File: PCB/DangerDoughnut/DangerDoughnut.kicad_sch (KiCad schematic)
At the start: 81 parts, among them J1 Conn_01x02_Pin, J2 Conn_01x02_Pin, J3 Conn_01x02_Pin, J4 Conn_01x04_Pin, J6 USB_C_Receptacle_USB2.0_16P, U1 MMC5983MA, U10 ESP32-S3, U2 H3LIS331DLTR, U3 H3LIS331DLTR, U4 W25X20CLZP, U6 L5973D, U7 MIC5219-3.3YM5, U8 ESP8285H16, U9 SX1280IMLTRT, Y1 40MHz, Y2 52MHz, Y3 26MHz

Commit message: verified elsr
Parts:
- removed FL2: 2450FM07D0034T, Danger_Doughnut_Lib:FIL_2450FM07D0034T, symbol Danger_Doughnut_Lib:2450FM07D0034T
- removed R11: 0, Resistor_SMD:R_0603_1608Metric_Pad0.98x0.95mm_HandSolder, symbol Device:R
- added C29: 100uF, Capacitor_THT:CP_Radial_D6.3mm_P2.50mm, symbol Device:C_Polarized
- added D6: Green LED, LED_SMD:LED_0805_2012Metric, symbol Device:LED
- added R20: 30, Resistor_SMD:R_0402_1005Metric, symbol Device:R
- added R21, R22: 100, Resistor_SMD:R_0402_1005Metric, symbol Device:R
- C1, C11, C14, C16, C17, C2, C20, C21, C22, C23, C25, C26, C27, C28, C3, C30, C32, C33, C6, C7, C9: footprint Capacitor_SMD:C_0603_1608Metric_Pad1.08x0.95mm_HandSolder -> Capacitor_SMD:C_0402_1005Metric
- C8: footprint Capacitor_SMD:CP_Elec_6.3x7.7 -> Capacitor_THT:CP_Radial_D6.3mm_P2.50mm
- D2: footprint Diode_SMD:D_SOD-882D -> Diode_SMD:D_0805_2012Metric
- D3: footprint Diode_SMD:D_SOD-882D -> Capacitor_SMD:C_0805_2012Metric
- R1, R10, R12, R13, R14, R15, R16, R19, R2, R3, R4, R5, R6, R7, R8, R9: footprint Resistor_SMD:R_0603_1608Metric_Pad0.98x0.95mm_HandSolder -> Resistor_SMD:R_0402_1005Metric
- R17, R18: value 2.2K -> 3.3k; footprint Resistor_SMD:R_0603_1608Metric_Pad0.98x0.95mm_HandSolder -> Resistor_SMD:R_0402_1005Metric
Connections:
- net +3.3V: now also C21.1, U9.11 (VBAT_IO), R20.2
- net +5V: now also J4.3 (Pin_3); no longer J4.2 (Pin_2)
- net +BATT: now also C29.1
- net GND: now also J4.4 (Pin_4), C29.2; no longer J4.1 (Pin_1)
- net LED_MOSI: now also R21.2
- net LED_SCK: now also R22.2
- net ACCEL2_INT: now reaches U3.11 (INT1)
- net MAG_INT: now reaches U1.15 (INT)
- net ACCEL1_INT: now reaches U2.11 (INT1)
- new net: D6.2 (A), R20.1
- new net: J4.1 (Pin_1), R22.1
- new net: J4.2 (Pin_2), R21.1
- new net LED_BOTTOM: D6.1 (K)
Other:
- note added: "TODO: wire ESP32 uart resistor? find pinouts sensor interupts? add pin header add disconnects add test points add ground option elrs boot pin boot pins accessable Organize"
- note removed: "TODO: import HD107s LEDs wire LEDs wire ESP32 uart resistor? find pinouts sensor interupts? add pin header add disconnects add test points boot pins accessable Organize"

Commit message: updated schematic
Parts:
- added C34: 1.8pF, Capacitor_SMD:C_0402_1005Metric, symbol Device:C
- added C35: 1.2pF, Capacitor_SMD:C_0402_1005Metric, symbol Device:C
- added C36: 1uF, Capacitor_SMD:C_0402_1005Metric, symbol Device:C
- added C41: 100nF, Capacitor_SMD:C_0603_1608Metric, symbol Device:C
- added L3: 3nH, Inductor_SMD:L_0402_1005Metric_Pad0.77x0.64mm_HandSolder, symbol Device:L
- added R11: 10K, Resistor_SMD:R_0402_1005Metric, symbol Device:R
- added R25: 510, Resistor_SMD:R_0402_1005Metric, symbol Device:R
- added SW1, SW2: SW_Push, Button_Switch_SMD:SW_Push_1P1T_XKB_TS-1187A, symbol Switch:SW_Push
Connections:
- net +3.3V: now also R11.1
- net ACCEL1_INT: now also U10.8 (GPIO3)
- net ACCEL2_INT: now also U10.7 (GPIO2)
- net Accel1_CS: now also U10.11 (GPIO6)
- net Accel2_CS: now also U10.12 (GPIO7)
- net ELSR_RX: now also R25.2
- net ELSR_TX: now also U10.50 (U0RXD)
- net GND: now also C34.2, C35.2, C36.2, SW2.1
- net LED_BOTTOM: now also U10.16 (GPIO11)
- net MAG_INT: now also U10.9 (GPIO4)
- net Mag_CS: now also U10.10 (GPIO5)
- net at U10.1 (LNA_IN): now also C34.1, L3.1
- net ESP_RST: now reaches U10.4 (CHIP_PU)
- net ESP_RST: now also C36.1, C41.1, R11.2, SW1.1
- net at U10.49 (U0TXD): now also R25.1
- net at U10.5 (GPIO0): now also SW2.2
- net at ANT2.2 (FEED): now also C35.1, L3.2
- new net: C41.2, SW1.2
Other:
- note added: "TODO: add pin header add disconnects add test points add ground option elrs boot pin boot pins accessable Organize"
- note removed: "TODO: wire ESP32 uart resistor? find pinouts sensor interupts? add pin header add disconnects add test points add ground option elrs boot pin boot pins accessable Organize"
- moved on the sheet: ANT2

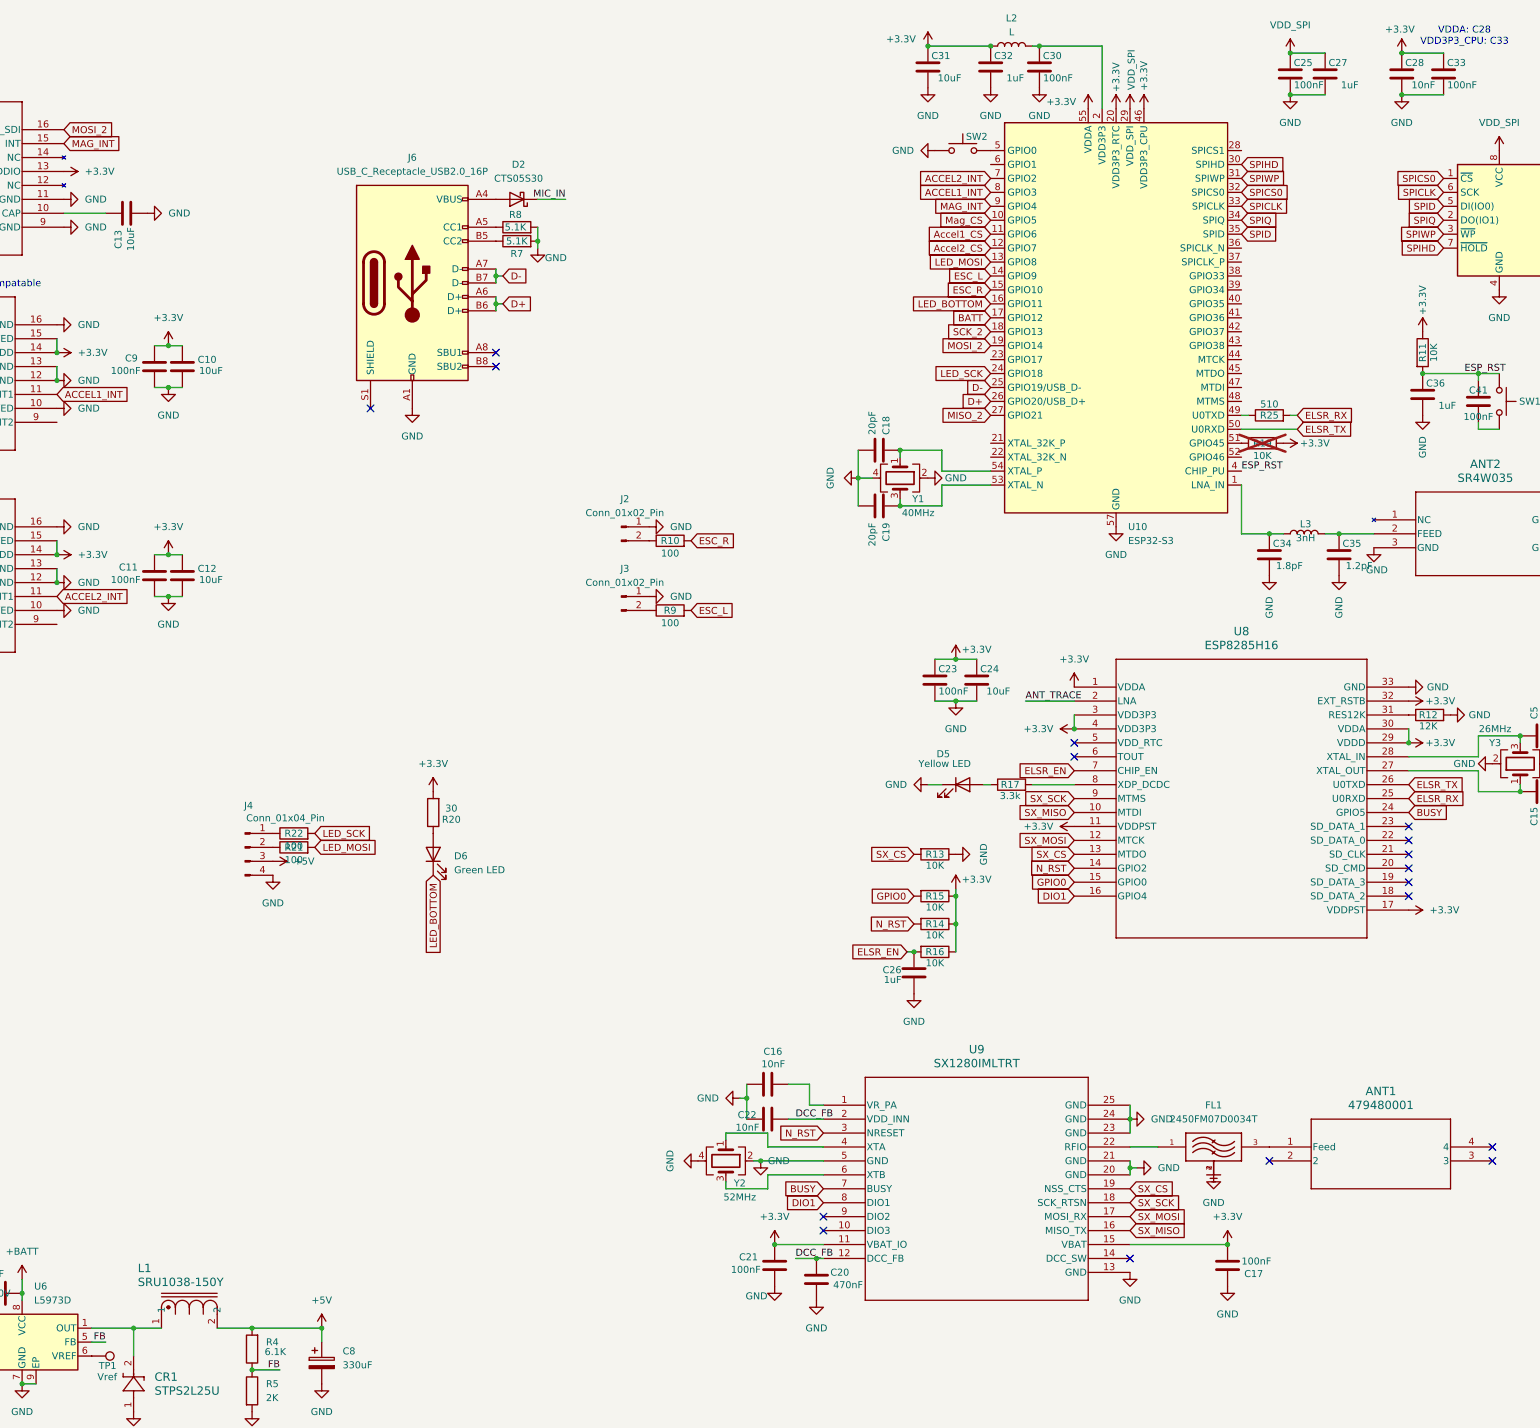
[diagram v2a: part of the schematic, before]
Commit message: updated schematic power layout done
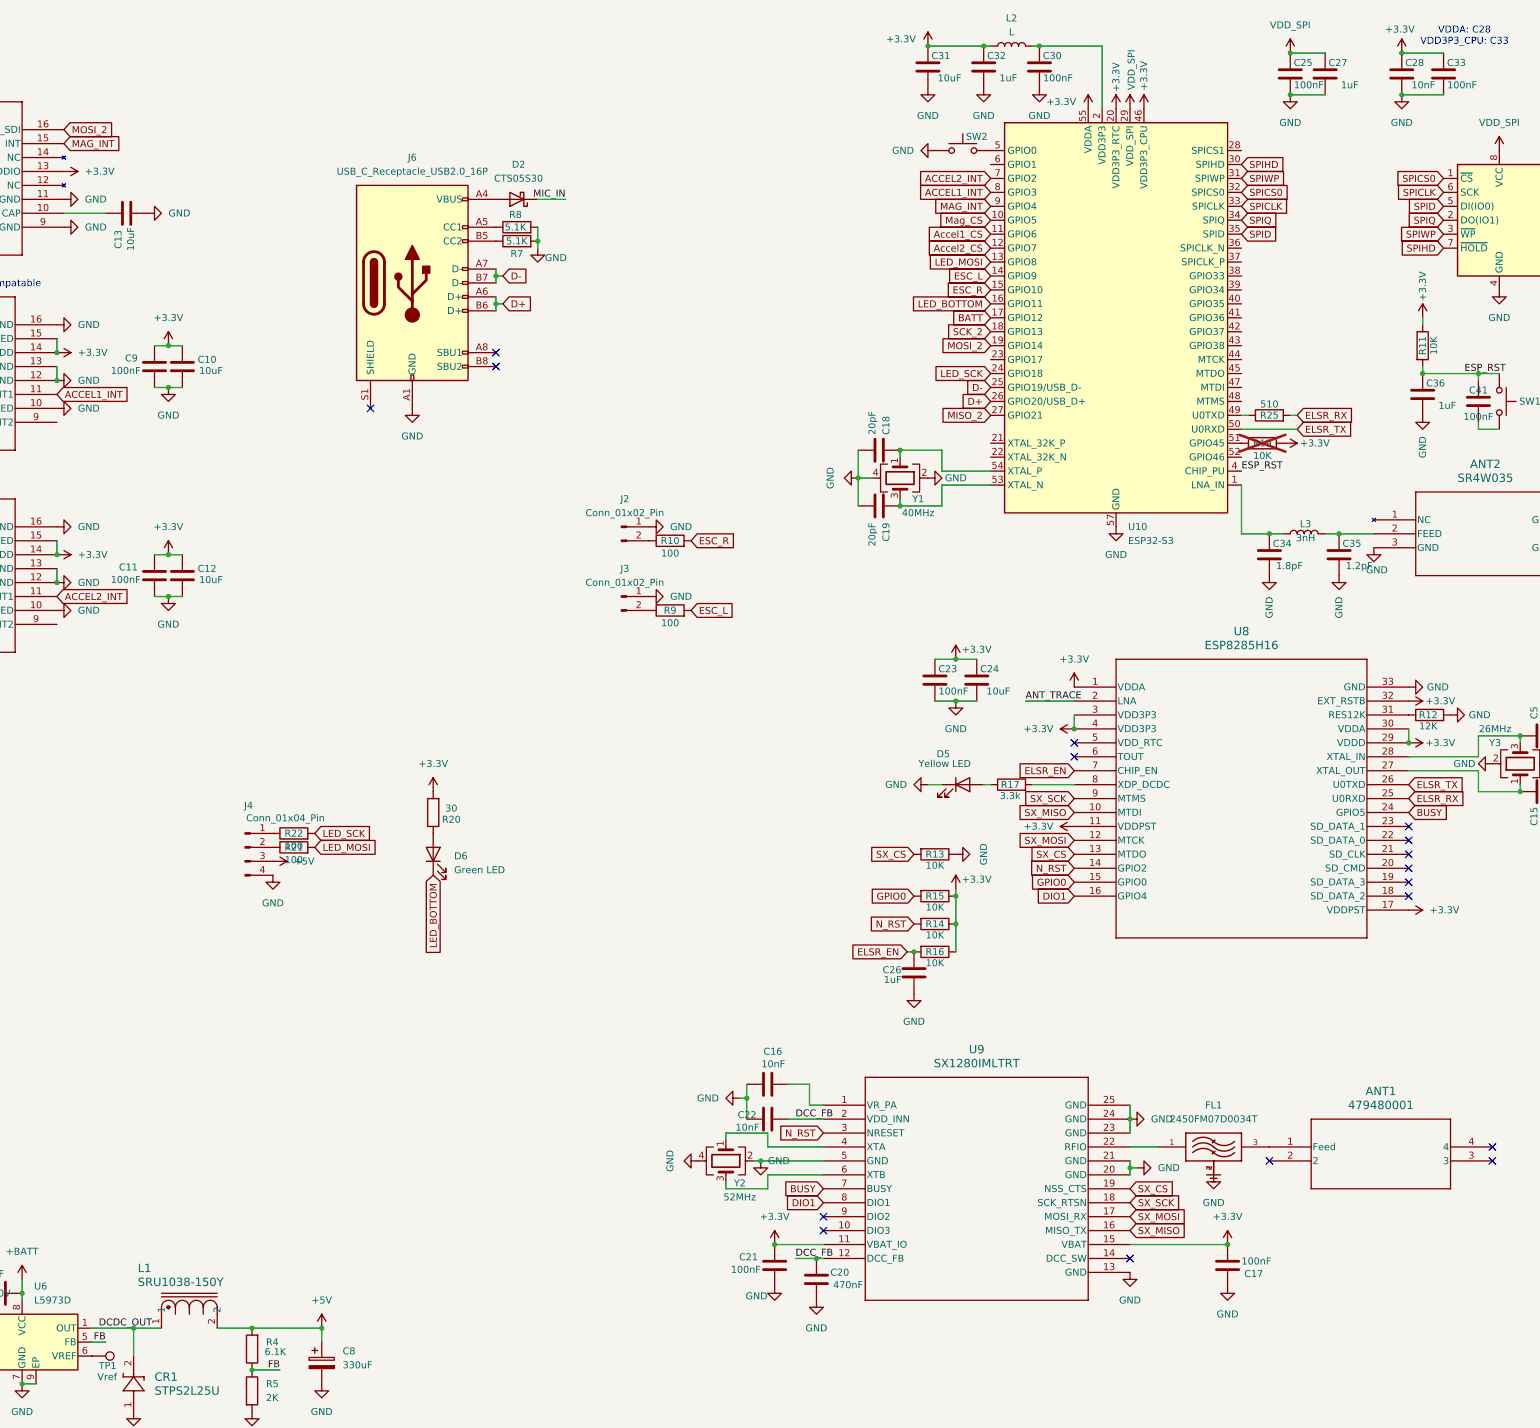
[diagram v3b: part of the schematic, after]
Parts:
- D3: footprint Capacitor_SMD:C_0805_2012Metric -> Diode_SMD:D_0805_2012Metric
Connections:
- net DCDC_OUT: now reaches CR1.2, L1.1, U6.1 (OUT)
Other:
- moved on the sheet: C32, R11
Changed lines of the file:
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@@
 	)
 	(junction
-		(at 292.1 17.78)
+		(at 290.83 17.78)
 		(diameter 0)
 		(color 0 0 0 0)
@@
 	(wire
 		(pts
+			(xy 370.84 67.31) (xy 370.84 68.58)
+		)
+		(stroke
+			(width 0)
+			(type default)
+		)
+	)
+	(wire
+		(pts
 			(xy 157.48 251.46) (xy 170.18 251.46)
 		)
@@
 	(wire
 		(pts
+			(xy 290.83 17.78) (xy 292.1 17.78)
+		)
+		(stroke
+			(width 0)
+			(type default)
+		)
+	)
+	(wire
+		(pts
 			(xy 281.94 137.16) (xy 285.75 137.16)
 		)
@@
 	(wire
 		(pts
-			(xy 280.67 17.78) (xy 292.1 17.78)
+			(xy 280.67 17.78) (xy 290.83 17.78)
 		)
 		(stroke
@@
 	(wire
 		(pts
+			(xy 370.84 76.2) (xy 370.84 77.47)
+		)
+		(stroke
+			(width 0)
+			(type default)
+		)
+	)
+	(wire
+		(pts
 			(xy 102.87 271.78) (xy 102.87 273.05)
 		)
@@
 		)
 	)
+	(label "DCDC_OUT"
+		(at 129.54 251.46 0)
+		(fields_autoplaced yes)
+		(effects
+			(font
+				(size 1.27 1.27)
+			)
+			(justify left bottom)
+		)
+	)
 	(label "ANT_TRACE"
 		(at 298.45 137.16 0)
@@
 			)
 		)
-		(property "Footprint" "Capacitor_SMD:C_0805_2012Metric"
+		(property "Footprint" "Diode_SMD:D_0805_2012Metric"
 			(at 34.29 243.84 0)
 			(effects
@@
 	(symbol
 		(lib_id "power:GND")
-		(at 292.1 25.4 0)
+		(at 290.83 25.4 0)
 		(unit 1)
 		(exclude_from_sim no)
@@
 		(fields_autoplaced yes)
 		(property "Reference" "#PWR095"
-			(at 292.1 31.75 0)
+			(at 290.83 31.75 0)
 			(effects
 				(font
@@
 		)
 		(property "Value" "GND"
-			(at 292.1 30.48 0)
+			(at 290.83 30.48 0)
 			(effects
 				(font
@@
 		)
 		(property "Footprint" ""
-			(at 292.1 25.4 0)
+			(at 290.83 25.4 0)
 			(effects
 				(font
@@
 		)
 		(property "Datasheet" ""
-			(at 292.1 25.4 0)
+			(at 290.83 25.4 0)
 			(effects
 				(font
@@
 		)
 		(property "Description" "Power symbol creates a global label with name \"GND\" , ground"
-			(at 292.1 25.4 0)
+			(at 290.83 25.4 0)
 			(effects
 				(font
@@
 	(symbol
 		(lib_id "Device:R")
-		(at 370.84 73.66 0)
+		(at 370.84 72.39 0)
 		(unit 1)
 		(exclude_from_sim no)
@@
 		(dnp no)
 		(property "Reference" "R11"
-			(at 370.84 73.66 90)
+			(at 370.84 72.39 90)
 			(effects
 				(font
@@
 		)
 		(property "Value" "10K"
-			(at 372.872 73.66 90)
+			(at 372.872 72.39 90)
 			(effects
 				(font
@@
 		)
 		(property "Footprint" "Resistor_SMD:R_0402_1005Metric"
-			(at 369.062 73.66 90)
+			(at 369.062 72.39 90)
 			(effects
 				(font
@@
 		)
 		(property "Datasheet" "~"
-			(at 370.84 73.66 0)
+			(at 370.84 72.39 0)
 			(effects
 				(font
@@
 		)
 		(property "Description" "Resistor"
-			(at 370.84 73.66 0)
+			(at 370.84 72.39 0)
 			(effects
 				(font
@@
 	(symbol
 		(lib_id "Device:C")
-		(at 292.1 21.59 0)
+		(at 290.83 21.59 0)
 		(unit 1)
 		(exclude_from_sim no)
@@
 		(dnp no)
 		(property "Reference" "C32"
-			(at 296.164 19.558 0)
+			(at 294.894 19.558 0)
 			(effects
 				(font
@@
 		)
 		(property "Value" "1uF"
-			(at 298.196 23.622 0)
+			(at 296.926 23.622 0)
 			(effects
 				(font
@@
 		)
 		(property "Footprint" "Capacitor_SMD:C_0402_1005Metric"
-			(at 293.0652 25.4 0)
+			(at 291.7952 25.4 0)
 			(effects
 				(font
@@
 		)
 		(property "Datasheet" "~"
-			(at 292.1 21.59 0)
+			(at 290.83 21.59 0)
 			(effects
 				(font
@@
 		)
 		(property "Description" "Unpolarized capacitor"
-			(at 292.1 21.59 0)
+			(at 290.83 21.59 0)
 			(effects
 				(font
@@
 	(symbol
 		(lib_id "power:+3.3V")
-		(at 370.84 69.85 0)
+		(at 370.84 67.31 0)
 		(unit 1)
 		(exclude_from_sim no)
@@
 		(dnp no)
 		(property "Reference" "#PWR0104"
-			(at 370.84 73.66 0)
+			(at 370.84 71.12 0)
 			(effects
 				(font
@@
 		)
 		(property "Value" "+3.3V"
-			(at 370.84 66.802 90)
+			(at 370.84 64.262 90)
 			(effects
 				(font
@@
 		)
 		(property "Footprint" ""
-			(at 370.84 69.85 0)
+			(at 370.84 67.31 0)
 			(effects
 				(font
@@
 		)
 		(property "Datasheet" ""
-			(at 370.84 69.85 0)
+			(at 370.84 67.31 0)
 			(effects
 				(font
@@
 		)
 		(property "Description" "Power symbol creates a global label with name \"+3.3V\""
-			(at 370.84 69.85 0)
+			(at 370.84 67.31 0)
 			(effects
 				(font
